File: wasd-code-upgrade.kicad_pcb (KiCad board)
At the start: 2 copper layers, 55 x 33 mm, 22 parts, among them J101 Conn_ARM_JTAG_SWD_10, J102 TC2030, Q101 ZXTN08400BFF, Q102 ZXTP25020CFFTA, U101 STM32L422CBTx, U102 MIC5205-3.3YM5

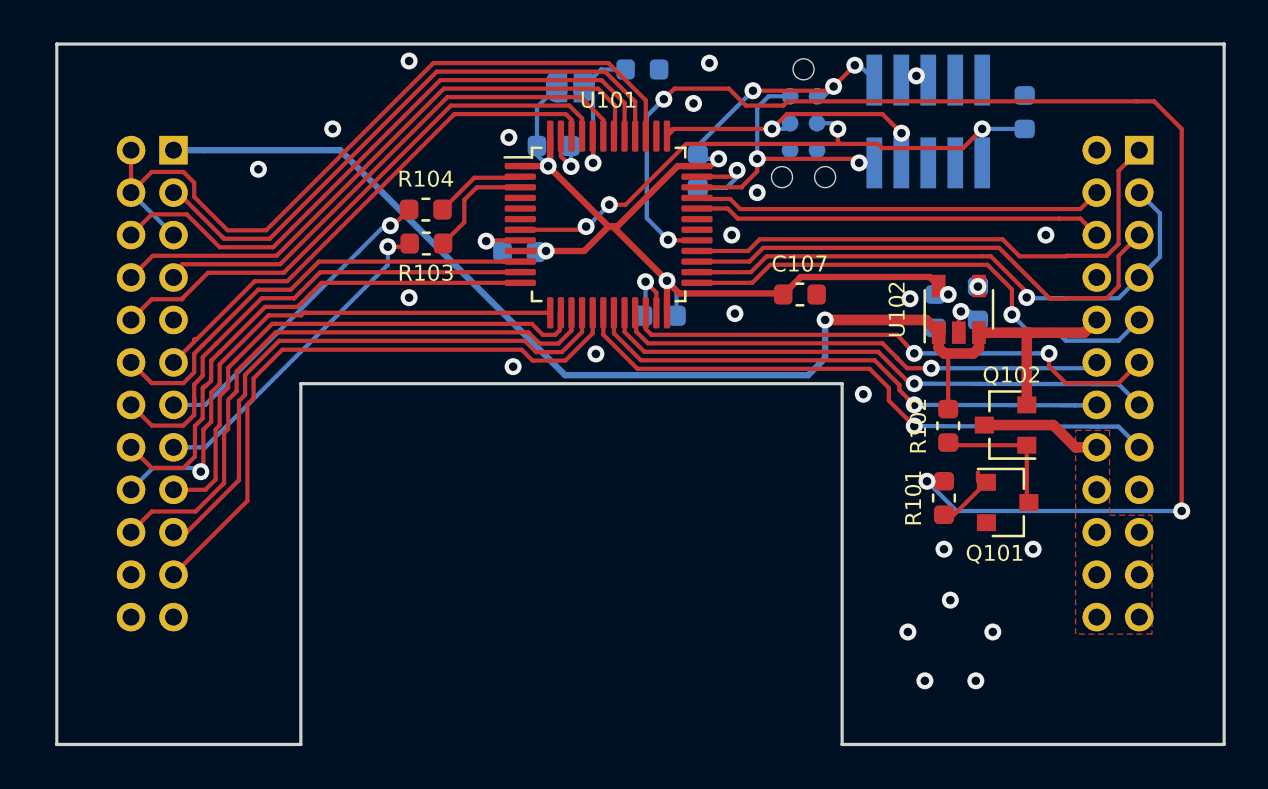
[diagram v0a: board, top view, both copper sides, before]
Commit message: wasd-code-upgrade: v2 layout
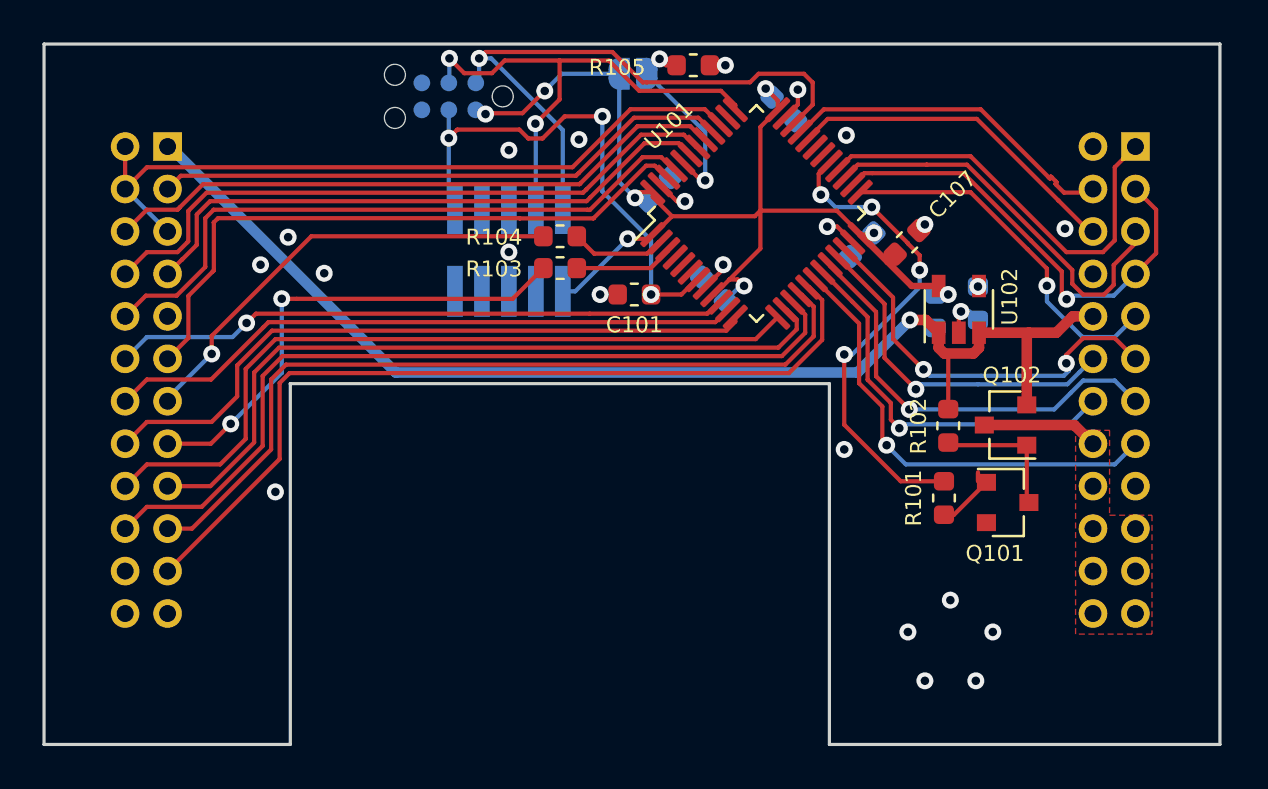
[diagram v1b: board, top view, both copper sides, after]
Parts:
- C101, R105: moved to F.Cu
- H201, H202: value Conn_02x12_Odd_Even -> Molex0877582416
- moved J101 20.7 mm to (112.3, 59.7), turned to 90 degrees
- moved C101 20.3 mm to (118.2, 61.8), turned to 180 degrees
- moved J102 16.8 mm to (109.5, 52.5), turned to 180 degrees
- moved C102 14.2 mm to (125.3, 53.1), turned to 315 degrees
- moved C103 10.1 mm to (128.9, 59.5), turned to 225 degrees
- moved U101 6.99 mm to (124.0, 58.0), turned to 45 degrees
- moved R104 6.45 mm to (114.7, 59.1)
- moved R103 6.41 mm to (114.7, 60.6)
- moved C107 5.61 mm to (131.1, 59.3), turned to 45 degrees
- moved C106 5.61 mm to (121.9, 61.5), turned to 135 degrees
- moved C104 5.35 mm to (119.4, 56.8), turned to 45 degrees
- moved JP101 3.01 mm to (118.2, 51.4)
- moved R105 2.41 mm to (121.0, 51.0)
- moved H202 0.33 mm to (96.2, 54.8)
- moved H201 0.25 mm to (141.8, 54.8)
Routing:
- net /BACKLIGHT_PWM: track 65.7 -> 23.1 mm
- net /SWDIO: track 13.5 -> 29.5 mm, vias 2 -> 1
- net /HIGH2: track 29.1 -> 40.3 mm
- net /HIGH1: track 27.2 -> 38.4 mm
- net /HIGH0: track 24.8 -> 35.8 mm
- net /HIGH7: track 28.6 -> 39.5 mm
- net /HIGH6: track 25.9 -> 36.0 mm, vias 1 -> 0
- net /SWCLK: track 14.7 -> 23.7 mm
- net Net-(H202-Pad15): track 15.1 -> 23.2 mm, vias 1 -> 2
- net /HIGH5: track 24.6 -> 32.2 mm
- net /LOW6: track 28.8 -> 21.7 mm
- net Net-(H202-Pad13): track 14.4 -> 21.5 mm
- net /HIGH4: track 23.2 -> 30.2 mm
- net /LOW4: track 25.9 -> 19.0 mm
- net /LOW8: track 25.3 -> 18.5 mm
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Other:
- board size 55 x 33 mm -> 55.4 x 33 mm
- net class Default: clearance 0.2 -> 0.19998
- rule trace_clearance: 0.2 -> 0.19998
- board text added: "2020-08-15 v2"
- board text removed: "2020-08-11 v1"
- board text removed: "OPEN CODE"

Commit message: wasd-code-upgrade: high side decoder simplifies routing
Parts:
- added U103: 74HC238, vssop:VSSOP-16_3.0x4.25mm_P0.5mm, F.Cu at (106.8, 63.6)
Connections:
- net /TIM1_CH2 renamed /I2C1_SCL
- net /TIM1_CH3 renamed /I2C1_SDA
- U101 pad 10: /HIGH3 -> Net-(U101-Pad10)
- U101 pad 11: /HIGH4 -> Net-(U101-Pad11)
- U101 pad 12: /HIGH5 -> Net-(U101-Pad12)
- U101 pad 13: /HIGH6 -> Net-(U101-Pad13)
- U101 pad 14: /HIGH0 -> /EH2
- U101 pad 15: /HIGH7 -> /EH1
- U101 pad 16: /HIGH1 -> /EH0
- U101 pad 17: /HIGH2 -> /BACKLIGHT_PWM
- U101 pad 29: /BACKLIGHT_PWM -> Net-(U101-Pad29)
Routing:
- net /HIGH2: track 40.3 -> 15.0 mm
- net /HIGH1: track 38.4 -> 14.2 mm
- net /HIGH7: track 39.5 -> 16.4 mm
- net /HIGH0: track 35.8 -> 13.8 mm
- net /EH0: track 0.00 -> 20.9 mm
- net /HIGH6: track 36.0 -> 16.0 mm
- net /EH1: track 0.00 -> 19.8 mm
- net /EH2: track 0.00 -> 18.7 mm
- net /HIGH5: track 32.2 -> 14.3 mm
- net /HIGH4: track 30.2 -> 12.8 mm
- net /HIGH3: track 29.1 -> 16.2 mm
- net +3V3: track 54.1 -> 66.1 mm, vias 8 -> 9
- net /BACKLIGHT_PWM: track 23.1 -> 13.1 mm, vias 4 -> 0

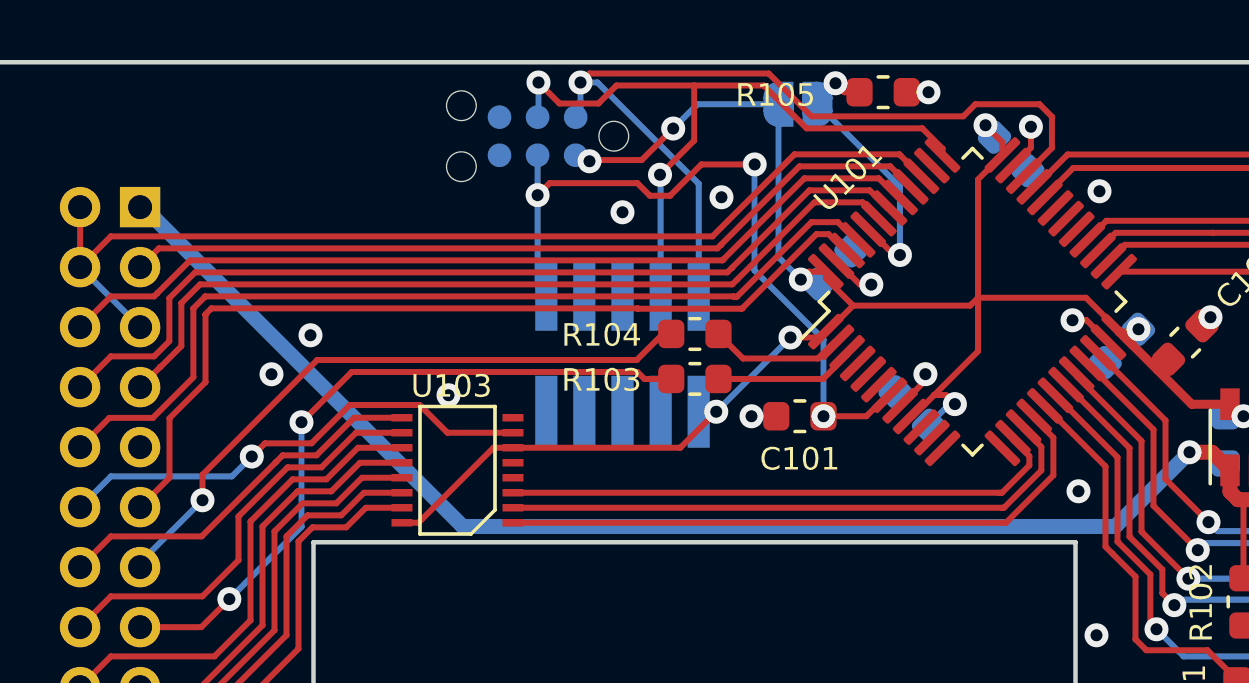
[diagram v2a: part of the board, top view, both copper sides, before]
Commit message: wasd-code-upgrade: socket for MakerFocus OLED
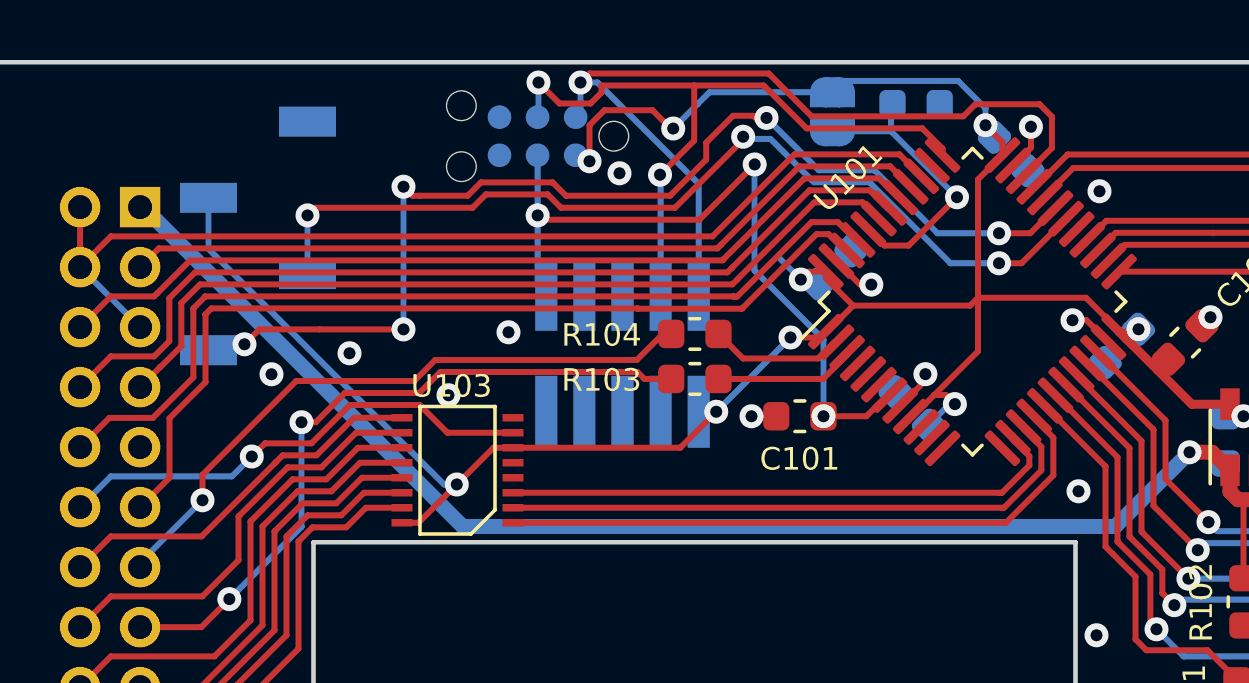
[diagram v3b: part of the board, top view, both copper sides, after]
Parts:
- added J103: OLED, Connector_PinSocket_2.54mm:PinSocket_1x04_P2.54mm_Vertical_SMD_Pin1Left, B.Cu at (100.2, 55.8)
- R105: moved to B.Cu
- U103: value 74HC238 -> TC74VHC238F
- moved JP101 1.18 mm to (119.3, 51.6), turned to 270 degrees
- moved R105 1.17 mm to (122.1, 51.4)
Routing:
- net /I2C1_SDA: track 0.00 -> 37.2 mm, vias 0 -> 5
- net /I2C1_SCL: track 0.00 -> 31.1 mm, vias 0 -> 3
- net +3V3: track 66.1 -> 83.4 mm, vias 9 -> 10
- net GND: track 9.08 -> 8.35 mm, vias 23 -> 22
- net /BOOT0: track 9.45 -> 9.87 mm, vias 2 -> 1

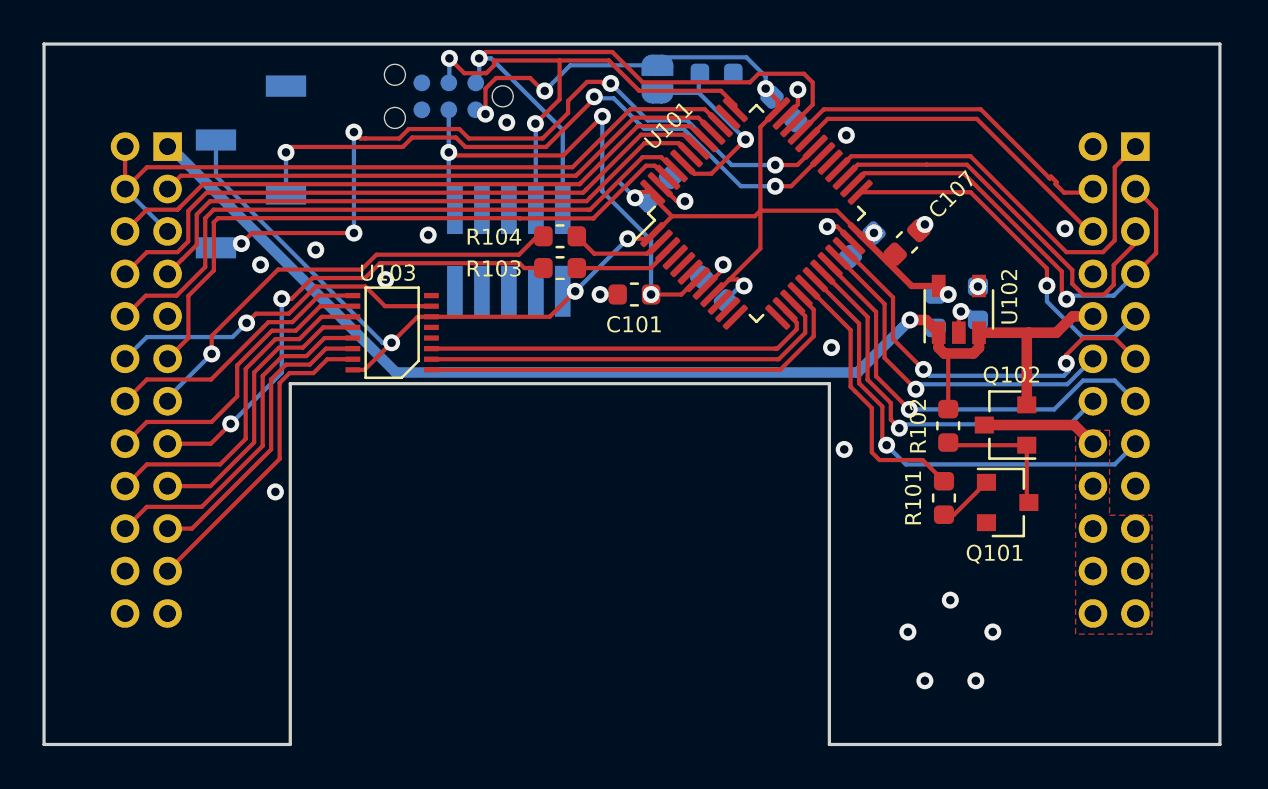
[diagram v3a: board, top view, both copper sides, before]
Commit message: wasd-code-upgrade: rework after playing with v1
- Move _very bright_ status LEDs to PWM-capable pins.
- Fix mistakes in matrix.
- Simplify some layout to move more things to topside.
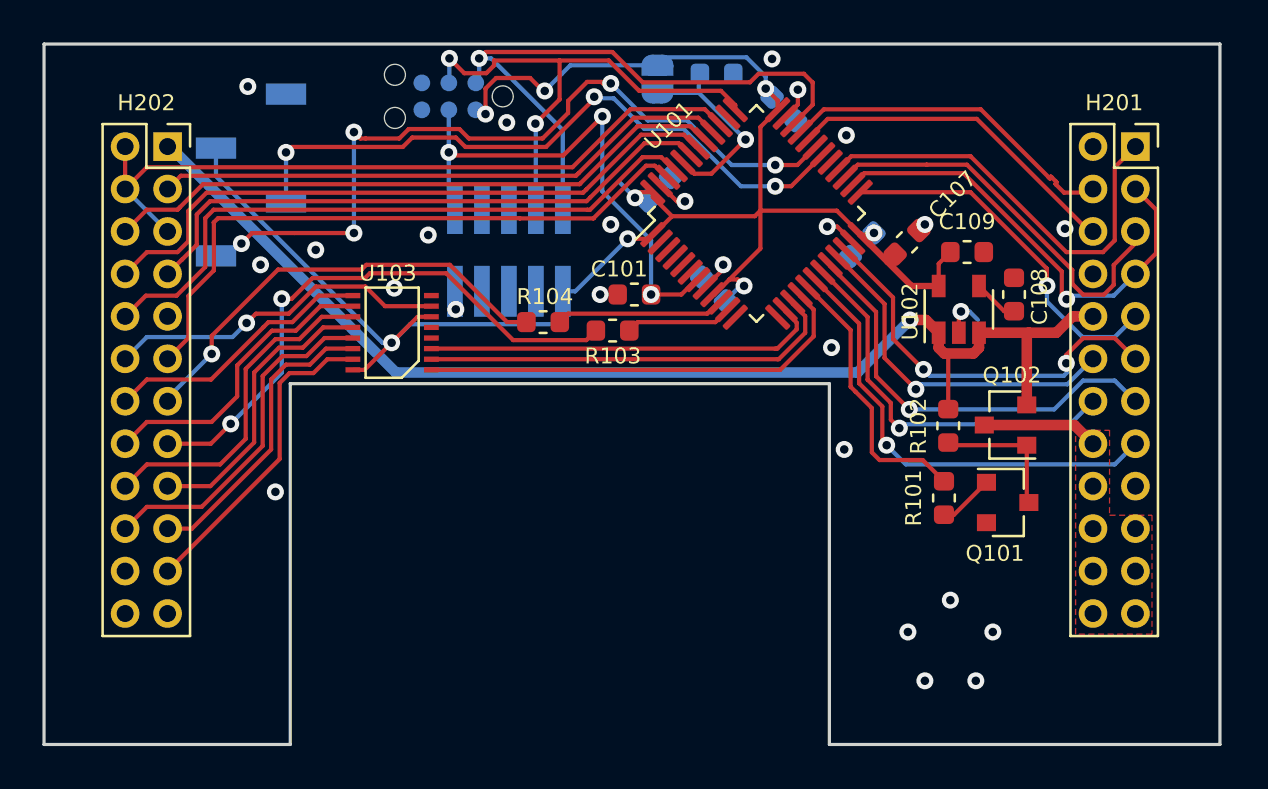
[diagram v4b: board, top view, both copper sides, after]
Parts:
- C108, C109, H201, H202: moved to F.Cu
- moved R104 4.12 mm to (113.9, 63.1)
- moved R103 3.85 mm to (117.2, 63.5)
- moved C109 3.16 mm to (133.9, 59.8), turned to 0 degrees
- moved H201 2.00 mm to (139.8, 54.8), turned to 0 degrees
- moved H202 2.00 mm to (94.2, 54.8), turned to 0 degrees
- moved C108 1.75 mm to (136.1, 61.8), turned to 90 degrees
- moved J103 0.38 mm to (100.2, 56.2)
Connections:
- U101 pad 10: Net-(U101-Pad10) -> /STATUS1
- U101 pad 11: Net-(U101-Pad11) -> /STATUS0
- U101 pad 2: /STATUS1 -> Net-(U101-Pad2)
- U101 pad 3: /STATUS0 -> Net-(U101-Pad3)
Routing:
- net Net-(H202-Pad15): track 23.4 -> 27.0 mm
- net /STATUS1: track 4.50 -> 7.95 mm
- net +3V3: track 83.4 -> 86.6 mm, vias 10 -> 8
- net Net-(C108-Pad1): track 0.06 -> 2.14 mm, vias 1 -> 0
- net GND: vias 22 -> 26
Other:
- board text added: "2020-08-20 v2"
- board text added: "deCODE"
- board text removed: "2020-08-15 v2"
